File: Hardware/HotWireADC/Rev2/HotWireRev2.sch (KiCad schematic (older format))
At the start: 42 parts

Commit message: added footprints to schematic
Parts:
- added CON1: BARREL_JACK, Connect:JACK_ALIM, symbol BARREL_JACK
- added P1, P2, P3, P4: BNC, Connect:bnc-ci, symbol BNC
- added P5: CONN_02X06, Socket_Strips:Socket_Strip_Straight_2x06, symbol CONN_02X06
- C1, C10, C11, C13, C14, C15, C16, C17, C2, C3, C4, C5, C6, C7, C8: renamed from C?; footprint (none) -> Capacitors_SMD:C_1206_HandSoldering
- C12, C9: renamed from C?; footprint (none) -> Capacitors_Tantalum_SMD:TantalC_SizeU_EIA-6032
- JP1, JP3, JP4: renamed from JP?; footprint (none) -> Socket_Strips:Socket_Strip_Straight_1x03
- JP2: renamed from JP?; footprint (none) -> Socket_Strips:Socket_Strip_Straight_1x02
- R1, R10, R11, R2, R3, R4, R5, R6, R7, R8, R9: renamed from R?; footprint (none) -> Resistors_SMD:R_1206_HandSoldering
- SW1: renamed from SW?; footprint (none) -> Buttons_Switches_SMD:SW_SPST_EVPBF
- U1, U2, U3, U4, U8: renamed from U?; footprint (none) -> TO_SOT_Packages_SMD:SOT-23-5
- U5: renamed from U?; footprint (none) -> Housings_SSOP:TSSOP-24_4.4x7.8mm_Pitch0.65mm
- U6: renamed from U?; value 78L05 -> TL750L05; footprint (none) -> TO_SOT_Packages_THT:TO-92_Molded_Wide_Oval
- U7: renamed from U?; value 78L05 -> L78S05; footprint (none) -> TO_SOT_Packages_THT:TO-220_Neutral123_Vertical_LargePads
- U9: renamed from U?; footprint (none) -> SMD_Packages:SOIC-8-N
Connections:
- net EOC/~INT~/CDI is gone; now on net EXT_REF: U5.9 (EOC/~INT~/CDI)
- net GNDD is gone; now on net GNDA: C6.2, C8.2, SW1.2, U5.14 (DGND)
- net +3V3: now also P5.11 (P11), P5.12 (P12)
- net +5VA: now also U8.2 (V-)
- net EXT_REF: now also P5.7 (P7)
- net FS/~CS: now also P5.6 (P6)
- net GNDA: now also U8.5 (V+), CON1.2, CON1.3, P1.2 (Ext), P2.2 (Ext), P3.2 (Ext), P4.2 (Ext), P5.10 (P10), P5.9 (P9)
- net IN1: now also P2.1 (In)
- net IN2: now also P1.1 (In)
- net IN3: now also P4.1 (In)
- net IN4: now also P3.1 (In)
- net SCLK: now also P5.5 (P5)
- net SDI: now also P5.3 (P3)
- net SDO: now also P5.4 (P4)
- net VCC: now also CON1.1
- net ~CONVST: now also P5.2 (P2)
- net ~RESET: now also P5.1 (P1)
- no-connect marks 4 -> 6
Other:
- note added: "LOW CURRENT MODE"
- note added: "OPTIONAL - HIGH CURRENT MODE"

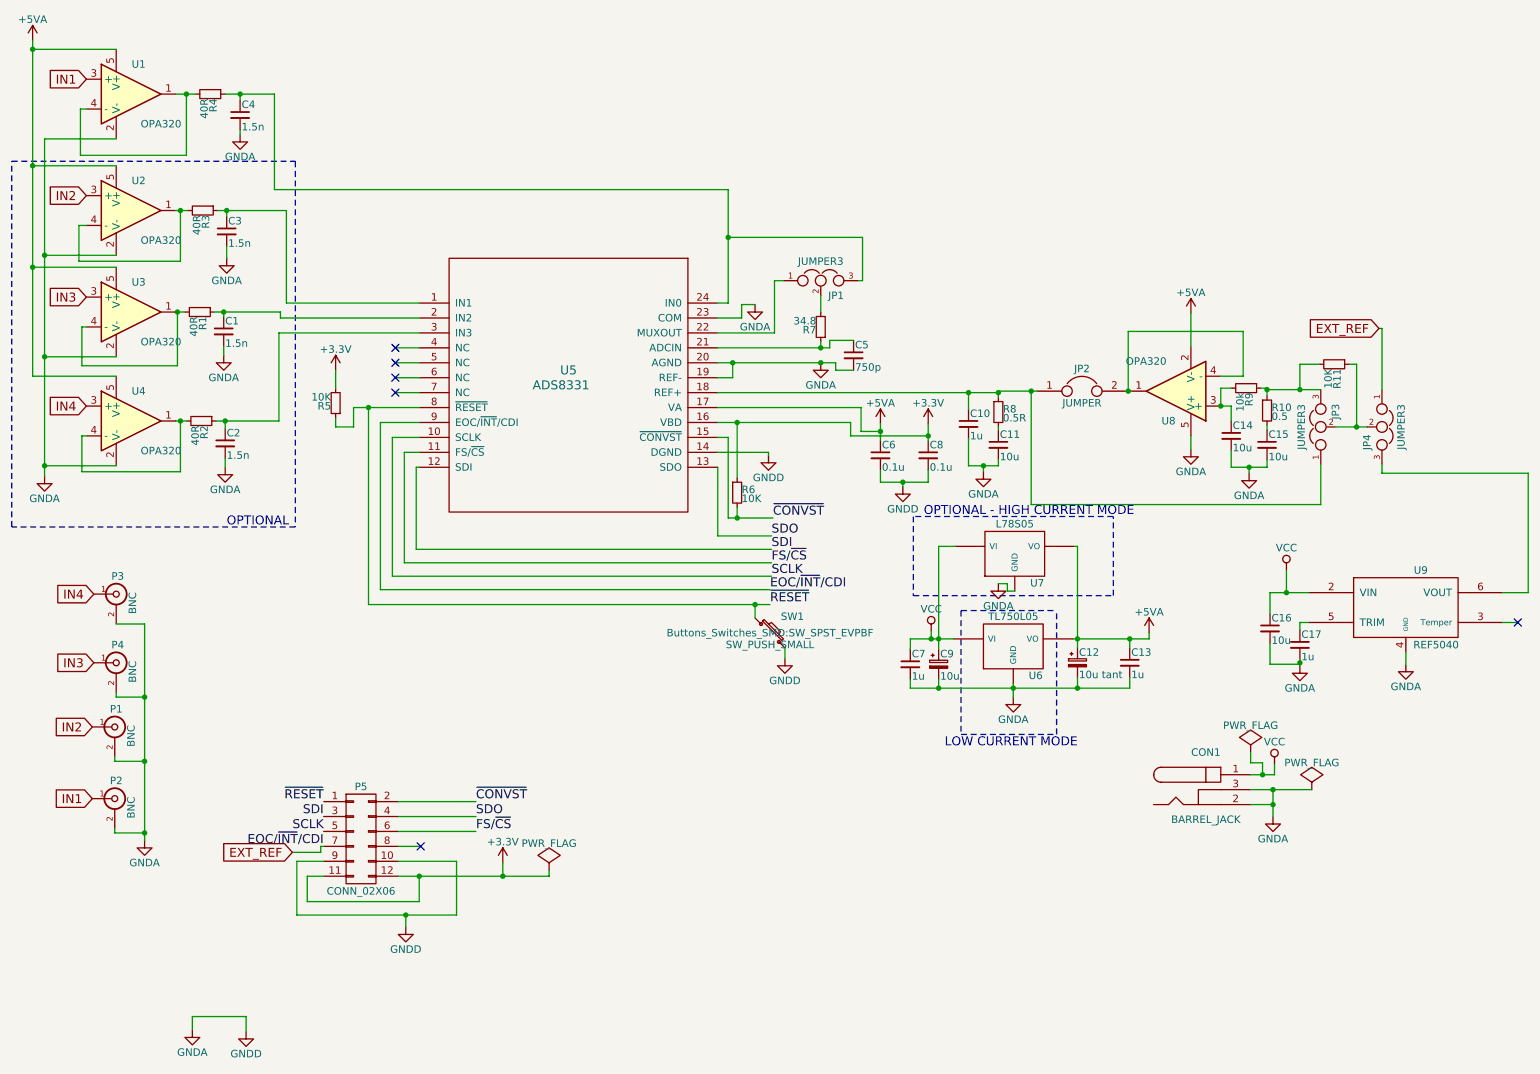
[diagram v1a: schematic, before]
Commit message: created intial PCB layout
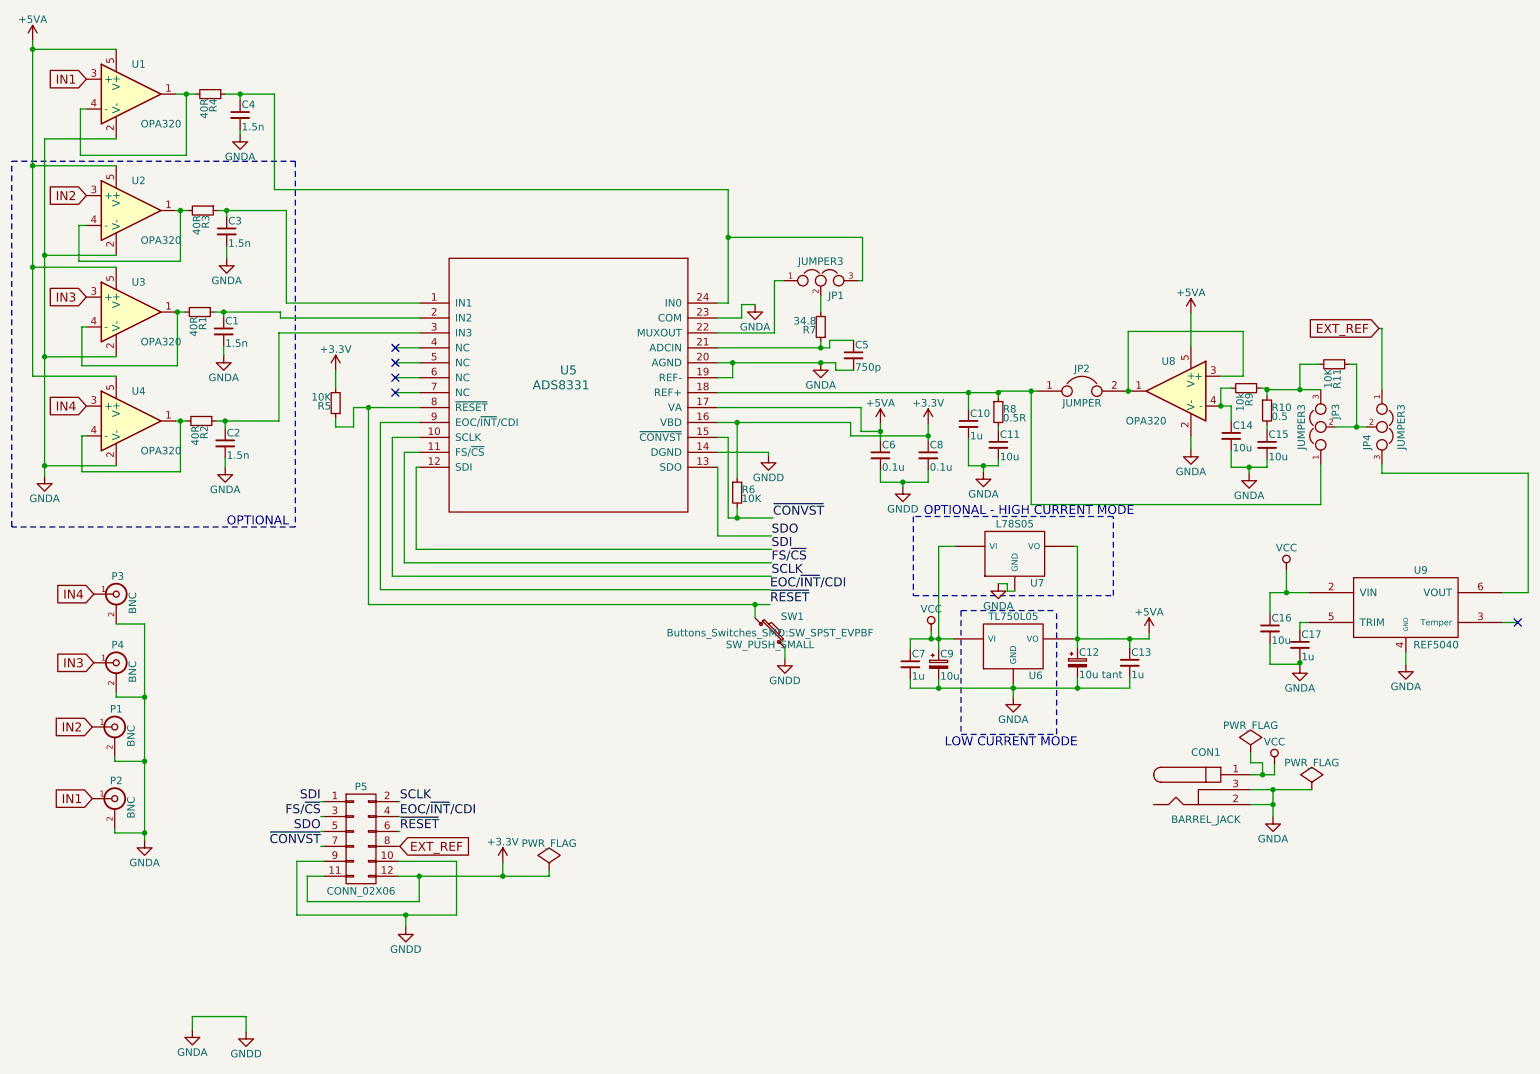
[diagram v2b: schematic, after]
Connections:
- net +5VA: now also U8.5 (V+); no longer U8.2 (V-)
- net EXT_REF: now also P5.8 (P8); no longer P5.7 (P7), U5.9 (EOC/~INT~/CDI)
- net FS/~CS: now also P5.3 (P3); no longer P5.6 (P6)
- net GNDA: now also U8.2 (V-); no longer U8.5 (V+)
- net SCLK: now also P5.2 (P2); no longer P5.5 (P5)
- net SDI: now also P5.1 (P1); no longer P5.3 (P3)
- net SDO: now also P5.5 (P5); no longer P5.4 (P4)
- net ~CONVST: now also P5.7 (P7); no longer P5.2 (P2)
- net ~RESET: now also P5.6 (P6); no longer P5.1 (P1)
- net at JP2.2, U8.1: now also U8.3 (+); no longer U8.4 (-)
- net at C14.1, R9.2: now also U8.4 (-); no longer U8.3 (+)
- new net EOC/~INT~/CDI: P5.4 (P4), U5.9 (EOC/~INT~/CDI)
- no-connect marks 6 -> 5
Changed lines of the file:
@@
 F 3 "" H 8360 3230 50  0000 C CNN
 	1    8310 3030
-	-1   0    0    1
+	-1   0    0    -1
 $EndComp
 Wire Wire Line
@@
 $EndComp
 Wire Wire Line
-	3100 5780 3620 5780
-Wire Wire Line
-	3100 5880 3620 5880
+	3100 5780 3110 5780
+Wire Wire Line
+	3100 5880 3110 5880
 Wire Wire Line
 	3100 6280 4110 6280
@@
 	3100 6180 3490 6180
 Wire Wire Line
-	3490 6180 3490 6540
+	3490 6540 3490 6180
 Wire Wire Line
 	2420 6540 2420 6180
@@
 	2080 7220 2080 7320
 Wire Wire Line
-	3490 6540 2420 6540
-Text Label 3620 5780 0    60   ~ 0
+	2420 6540 3490 6540
+Text Label 2580 6080 2    60   ~ 0
 ~CONVST
-Text Label 2600 5780 2    60   ~ 0
+Text Label 3110 5980 0    60   ~ 0
 ~RESET
-Text Label 3620 5880 0    60   ~ 0
+Text Label 2580 5980 2    60   ~ 0
 SDO
-Text Label 2600 5880 2    60   ~ 0
+Text Label 2580 5780 2    60   ~ 0
 SDI
-Text Label 3620 5980 0    60   ~ 0
+Text Label 2580 5880 2    60   ~ 0
 FS/~CS
-Text Label 2600 5980 2    60   ~ 0
+Text Label 3110 5780 0    60   ~ 0
 SCLK
-Text Label 2600 6080 2    60   ~ 0
+Text Label 3110 5880 0    60   ~ 0
 EOC/~INT~/CDI
 Wire Wire Line
-	3100 5980 3620 5980
-Wire Wire Line
-	3100 6080 3250 6080
-Wire Wire Line
-	2600 6080 2580 6080
-NoConn ~ 3250 6080
+	3100 5980 3110 5980
+Wire Wire Line
+	3100 6080 3110 6080
 Wire Wire Line
 	10500 4580 10600 4580
 NoConn ~ 10600 4580
-Text GLabel 2390 6120 0    60   Input ~ 0
+Text GLabel 3110 6080 2    60   Input ~ 0
 EXT_REF
-Wire Wire Line
-	2390 6120 2580 6120
-Wire Wire Line
-	2580 6120 2580 6080
 $Comp
 L GNDA #PWR034
@@
 Text Notes 6760 5420 0    60   ~ 0
 LOW CURRENT MODE
+Wire Wire Line
+	2600 5880 2580 5880
+Wire Wire Line
+	2580 5980 2600 5980
+Wire Wire Line
+	2600 6080 2580 6080
+Wire Wire Line
+	2600 5780 2580 5780
 $EndSCHEMATC

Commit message: moved external reference to BNC connector & tidied layout
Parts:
- added P6: BNC, Connect:bnc-ci, symbol BNC
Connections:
- net EXT_REF: now also P6.1 (In); no longer P5.8 (P8)
- net GNDA: now also P6.2 (Ext)
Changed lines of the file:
@@
 	5240 2740 5990 2740
 $Comp
-L GNDA #PWR01
+L GNDA #PWR14
 U 1 1 56E3F601
 P 5490 2450
-F 0 "#PWR01" H 5490 2200 50  0001 C CNN
+F 0 "#PWR14" H 5490 2200 50  0001 C CNN
 F 1 "GNDA" H 5490 2300 50  0000 C CNN
 F 2 "" H 5490 2450 50  0000 C CNN
@@
 	2040 1040 2040 1080
 $Comp
-L GNDA #PWR02
+L GNDA #PWR8
 U 1 1 56E40FF4
 P 2040 1310
-F 0 "#PWR02" H 2040 1060 50  0001 C CNN
+F 0 "#PWR8" H 2040 1060 50  0001 C CNN
 F 1 "GNDA" H 2040 1160 50  0000 C CNN
 F 2 "" H 2040 1310 50  0000 C CNN
@@
 $EndComp
 $Comp
-L GNDA #PWR03
+L GNDA #PWR7
 U 1 1 56E41956
 P 1950 2140
-F 0 "#PWR03" H 1950 1890 50  0001 C CNN
+F 0 "#PWR7" H 1950 1890 50  0001 C CNN
 F 1 "GNDA" H 1950 1990 50  0000 C CNN
 F 2 "" H 1950 2140 50  0000 C CNN
@@
 $EndComp
 $Comp
-L GNDA #PWR04
+L GNDA #PWR5
 U 1 1 56E41985
 P 1930 2790
-F 0 "#PWR04" H 1930 2540 50  0001 C CNN
+F 0 "#PWR5" H 1930 2540 50  0001 C CNN
 F 1 "GNDA" H 1930 2640 50  0000 C CNN
 F 2 "" H 1930 2790 50  0000 C CNN
@@
 $EndComp
 $Comp
-L GNDA #PWR05
+L GNDA #PWR6
 U 1 1 56E41CBD
 P 1940 3540
-F 0 "#PWR05" H 1940 3290 50  0001 C CNN
+F 0 "#PWR6" H 1940 3290 50  0001 C CNN
 F 1 "GNDA" H 1940 3390 50  0000 C CNN
 F 2 "" H 1940 3540 50  0000 C CNN
@@
 Connection ~ 730  2800
 $Comp
-L GNDA #PWR06
+L GNDA #PWR2
 U 1 1 56E467C4
 P 730 3600
-F 0 "#PWR06" H 730 3350 50  0001 C CNN
+F 0 "#PWR2" H 730 3350 50  0001 C CNN
 F 1 "GNDA" H 730 3450 50  0000 C CNN
 F 2 "" H 730 3600 50  0000 C CNN
@@
 IN4
 $Comp
-L +5VA #PWR07
+L +5VA #PWR1
 U 1 1 56E47E9A
 P 650 680
-F 0 "#PWR07" H 650 530 50  0001 C CNN
+F 0 "#PWR1" H 650 530 50  0001 C CNN
 F 1 "+5VA" H 650 820 50  0000 C CNN
 F 2 "" H 650 680 50  0000 C CNN
@@
 Connection ~ 650  740
 $Comp
-L GNDA #PWR08
+L GNDA #PWR17
 U 1 1 56E4881E
 P 5930 2840
-F 0 "#PWR08" H 5930 2590 50  0001 C CNN
+F 0 "#PWR17" H 5930 2590 50  0001 C CNN
 F 1 "GNDA" H 5930 2690 50  0000 C CNN
 F 2 "" H 5930 2840 50  0000 C CNN
@@
 ~RESET
 $Comp
-L GNDD #PWR09
+L GNDD #PWR19
 U 1 1 56E4A9FC
 P 6480 3670
-F 0 "#PWR09" H 6480 3420 50  0001 C CNN
+F 0 "#PWR19" H 6480 3420 50  0001 C CNN
 F 1 "GNDD" H 6480 3520 50  0000 C CNN
 F 2 "" H 6480 3670 50  0000 C CNN
@@
 $EndComp
 $Comp
-L GNDD #PWR010
+L GNDD #PWR16
 U 1 1 56E51293
 P 5690 4820
-F 0 "#PWR010" H 5690 4570 50  0001 C CNN
+F 0 "#PWR16" H 5690 4570 50  0001 C CNN
 F 1 "GNDD" H 5690 4670 50  0000 C CNN
 F 2 "" H 5690 4820 50  0000 C CNN
@@
 	5690 4750 5690 4820
 $Comp
-L +3.3V #PWR011
+L +3.3V #PWR20
 U 1 1 56E51B59
 P 6650 3250
-F 0 "#PWR011" H 6650 3100 50  0001 C CNN
+F 0 "#PWR20" H 6650 3100 50  0001 C CNN
 F 1 "+3.3V" H 6650 3390 50  0000 C CNN
 F 2 "" H 6650 3250 50  0000 C CNN
@@
 $EndComp
 $Comp
-L +3.3V #PWR012
+L +3.3V #PWR10
 U 1 1 56E51F06
 P 2680 2890
-F 0 "#PWR012" H 2680 2740 50  0001 C CNN
+F 0 "#PWR10" H 2680 2740 50  0001 C CNN
 F 1 "+3.3V" H 2680 3030 50  0000 C CNN
 F 2 "" H 2680 2890 50  0000 C CNN
@@
 $EndComp
 $Comp
-L +5VA #PWR013
+L +5VA #PWR18
 U 1 1 56E54038
 P 6330 3250
-F 0 "#PWR013" H 6330 3100 50  0001 C CNN
+F 0 "#PWR18" H 6330 3100 50  0001 C CNN
 F 1 "+5VA" H 6330 3390 50  0000 C CNN
 F 2 "" H 6330 3250 50  0000 C CNN
@@
 	5310 3340 5310 3880
 $Comp
-L GNDD #PWR014
+L GNDD #PWR15
 U 1 1 56E56979
 P 5580 3460
-F 0 "#PWR014" H 5580 3210 50  0001 C CNN
+F 0 "#PWR15" H 5580 3210 50  0001 C CNN
 F 1 "GNDD" H 5580 3310 50  0000 C CNN
 F 2 "" H 5580 3460 50  0000 C CNN
@@
 Connection ~ 6650 3330
 $Comp
-L GNDA #PWR015
+L GNDA #PWR22
 U 1 1 56E5B194
 P 7020 3570
-F 0 "#PWR015" H 7020 3320 50  0001 C CNN
+F 0 "#PWR22" H 7020 3320 50  0001 C CNN
 F 1 "GNDA" H 7020 3420 50  0000 C CNN
 F 2 "" H 7020 3570 50  0000 C CNN
@@
 	8920 3540 8920 3490
 $Comp
-L GNDA #PWR016
+L GNDA #PWR28
 U 1 1 56E66816
 P 8800 3580
-F 0 "#PWR016" H 8800 3330 50  0001 C CNN
+F 0 "#PWR28" H 8800 3330 50  0001 C CNN
 F 1 "GNDA" H 8800 3430 50  0000 C CNN
 F 2 "" H 8800 3580 50  0000 C CNN
@@
 $EndComp
 $Comp
-L GNDA #PWR017
+L GNDA #PWR33
 U 1 1 56E6DC74
 P 9850 4860
-F 0 "#PWR017" H 9850 4610 50  0001 C CNN
+F 0 "#PWR33" H 9850 4610 50  0001 C CNN
 F 1 "GNDA" H 9850 4710 50  0000 C CNN
 F 2 "" H 9850 4860 50  0000 C CNN
@@
 $EndComp
 $Comp
-L GNDA #PWR018
+L GNDA #PWR32
 U 1 1 56E6FEF4
 P 9140 4870
-F 0 "#PWR018" H 9140 4620 50  0001 C CNN
+F 0 "#PWR32" H 9140 4620 50  0001 C CNN
 F 1 "GNDA" H 9140 4720 50  0000 C CNN
 F 2 "" H 9140 4870 50  0000 C CNN
@@
 Connection ~ 9140 4850
 $Comp
-L VCC #PWR019
+L VCC #PWR31
 U 1 1 56E73E38
 P 9050 4230
-F 0 "#PWR019" H 9050 4080 50  0001 C CNN
+F 0 "#PWR31" H 9050 4080 50  0001 C CNN
 F 1 "VCC" H 9050 4380 50  0000 C CNN
 F 2 "" H 9050 4230 50  0000 C CNN
@@
 $EndComp
 $Comp
-L +5VA #PWR020
+L +5VA #PWR25
 U 1 1 56E766A8
 P 8130 4650
-F 0 "#PWR020" H 8130 4500 50  0001 C CNN
+F 0 "#PWR25" H 8130 4500 50  0001 C CNN
 F 1 "+5VA" H 8130 4790 50  0000 C CNN
 F 2 "" H 8130 4650 50  0000 C CNN
@@
 $EndComp
 $Comp
-L VCC #PWR021
+L VCC #PWR21
 U 1 1 56E76726
 P 6670 4640
-F 0 "#PWR021" H 6670 4490 50  0001 C CNN
+F 0 "#PWR21" H 6670 4490 50  0001 C CNN
 F 1 "VCC" H 6670 4790 50  0000 C CNN
 F 2 "" H 6670 4640 50  0000 C CNN
@@
 Connection ~ 8000 4690
 $Comp
-L GNDA #PWR022
+L GNDA #PWR24
 U 1 1 56E77814
 P 7220 5080
-F 0 "#PWR022" H 7220 4830 50  0001 C CNN
+F 0 "#PWR24" H 7220 4830 50  0001 C CNN
 F 1 "GNDA" H 7220 4930 50  0000 C CNN
 F 2 "" H 7220 5080 50  0000 C CNN
@@
 	6830 4070 6720 4070
 $Comp
-L GNDA #PWR023
+L GNDA #PWR23
 U 1 1 56E7EB42
 P 7120 4320
-F 0 "#PWR023" H 7120 4070 50  0001 C CNN
+F 0 "#PWR23" H 7120 4070 50  0001 C CNN
 F 1 "GNDA" H 7120 4170 50  0000 C CNN
 F 2 "" H 7120 4320 50  0000 C CNN
@@
 IN1
 $Comp
-L GNDA #PWR024
+L GNDA #PWR3
 U 1 1 56E89E10
 P 1400 6040
-F 0 "#PWR024" H 1400 5790 50  0001 C CNN
+F 0 "#PWR3" H 1400 5790 50  0001 C CNN
 F 1 "GNDA" H 1400 5890 50  0000 C CNN
 F 2 "" H 1400 6040 50  0000 C CNN
@@
 	3100 6180 3490 6180
 Wire Wire Line
-	3490 6540 3490 6180
+	3490 6180 3490 6540
 Wire Wire Line
 	2420 6540 2420 6180
@@
 Connection ~ 3240 6280
 $Comp
-L GNDA #PWR025
+L GNDA #PWR4
 U 1 1 56E8E642
 P 1720 7310
-F 0 "#PWR025" H 1720 7060 50  0001 C CNN
+F 0 "#PWR4" H 1720 7060 50  0001 C CNN
 F 1 "GNDA" H 1720 7160 50  0000 C CNN
 F 2 "" H 1720 7310 50  0000 C CNN
@@
 $EndComp
 $Comp
-L +3.3V #PWR026
+L +3.3V #PWR12
 U 1 1 56E902E0
 P 3800 6190
-F 0 "#PWR026" H 3800 6040 50  0001 C CNN
+F 0 "#PWR12" H 3800 6040 50  0001 C CNN
 F 1 "+3.3V" H 3800 6330 50  0000 C CNN
 F 2 "" H 3800 6190 50  0000 C CNN
@@
 $EndComp
 $Comp
-L GNDA #PWR027
+L GNDA #PWR29
 U 1 1 56E93599
 P 8960 5880
-F 0 "#PWR027" H 8960 5630 50  0001 C CNN
+F 0 "#PWR29" H 8960 5630 50  0001 C CNN
 F 1 "GNDA" H 8960 5730 50  0000 C CNN
 F 2 "" H 8960 5880 50  0000 C CNN
@@
 Connection ~ 8960 5800
 $Comp
-L VCC #PWR028
+L VCC #PWR30
 U 1 1 56E941B0
 P 8970 5530
-F 0 "#PWR028" H 8970 5380 50  0001 C CNN
+F 0 "#PWR30" H 8970 5380 50  0001 C CNN
 F 1 "VCC" H 8970 5680 50  0000 C CNN
 F 2 "" H 8970 5530 50  0000 C CNN
@@
 	8970 5600 8970 5530
 $Comp
-L PWR_FLAG #FLG029
+L PWR_FLAG #FLG2
 U 1 1 56E94ED5
 P 8810 5450
-F 0 "#FLG029" H 8810 5545 50  0001 C CNN
+F 0 "#FLG2" H 8810 5545 50  0001 C CNN
 F 1 "PWR_FLAG" H 8810 5630 50  0000 C CNN
 F 2 "" H 8810 5450 50  0000 C CNN
@@
 $EndComp
 $Comp
-L PWR_FLAG #FLG030
+L PWR_FLAG #FLG3
 U 1 1 56E95487
 P 9220 5700
-F 0 "#FLG030" H 9220 5795 50  0001 C CNN
+F 0 "#FLG3" H 9220 5795 50  0001 C CNN
 F 1 "PWR_FLAG" H 9220 5880 50  0000 C CNN
 F 2 "" H 9220 5700 50  0000 C CNN
@@
 $EndComp
 $Comp
-L PWR_FLAG #FLG031
+L PWR_FLAG #FLG1
 U 1 1 56E957F2
 P 4110 6240
-F 0 "#FLG031" H 4110 6335 50  0001 C CNN
+F 0 "#FLG1" H 4110 6335 50  0001 C CNN
 F 1 "PWR_FLAG" H 4110 6420 50  0000 C CNN
 F 2 "" H 4110 6240 50  0000 C CNN
@@
 Connection ~ 8890 5600
 $Comp
-L GNDD #PWR032
+L GNDD #PWR11
 U 1 1 56E9B38E
 P 3150 6620
-F 0 "#PWR032" H 3150 6370 50  0001 C CNN
+F 0 "#PWR11" H 3150 6370 50  0001 C CNN
 F 1 "GNDD" H 3150 6470 50  0000 C CNN
 F 2 "" H 3150 6620 50  0000 C CNN
@@
 Connection ~ 3150 6540
 $Comp
-L GNDD #PWR033
+L GNDD #PWR9
 U 1 1 56E9D5EC
 P 2080 7320
-F 0 "#PWR033" H 2080 7070 50  0001 C CNN
+F 0 "#PWR9" H 2080 7070 50  0001 C CNN
 F 1 "GNDD" H 2080 7170 50  0000 C CNN
 F 2 "" H 2080 7320 50  0000 C CNN
@@
 	2080 7220 2080 7320
 Wire Wire Line
-	2420 6540 3490 6540
+	3490 6540 2420 6540
 Text Label 2580 6080 2    60   ~ 0
 ~CONVST
@@
 	10500 4580 10600 4580
 NoConn ~ 10600 4580
-Text GLabel 3110 6080 2    60   Input ~ 0
+Text GLabel 4800 5920 0    60   Input ~ 0
 EXT_REF
 $Comp
-L GNDA #PWR034
+L GNDA #PWR27
 U 1 1 56EAC6C3
 P 8410 3420
-F 0 "#PWR034" H 8410 3170 50  0001 C CNN
+F 0 "#PWR27" H 8410 3170 50  0001 C CNN
 F 1 "GNDA" H 8410 3270 50  0000 C CNN
 F 2 "" H 8410 3420 50  0000 C CNN
@@
 	8410 3330 8410 3420
 $Comp
-L +5VA #PWR035
+L +5VA #PWR26
 U 1 1 56EAD0BF
 P 8410 2510
-F 0 "#PWR035" H 8410 2360 50  0001 C CNN
+F 0 "#PWR26" H 8410 2360 50  0001 C CNN
 F 1 "+5VA" H 8410 2650 50  0000 C CNN
 F 2 "" H 8410 2510 50  0000 C CNN
@@
 Wire Wire Line
 	2600 5780 2580 5780
+$Comp
+L BNC P6
+U 1 1 56E5B816
+P 4950 5920
+F 0 "P6" H 4960 6040 50  0000 C CNN
+F 1 "BNC" V 5060 5860 50  0000 C CNN
+F 2 "Connect:bnc-ci" H 4950 5920 50  0001 C CNN
+F 3 "" H 4950 5920 50  0000 C CNN
+	1    4950 5920
+	1    0    0    -1
+$EndComp
+$Comp
+L GNDA #PWR13
+U 1 1 56E5C590
+P 4950 6120
+F 0 "#PWR13" H 4950 5870 50  0001 C CNN
+F 1 "GNDA" H 4950 5970 50  0000 C CNN
+F 2 "" H 4950 6120 50  0000 C CNN
+F 3 "" H 4950 6120 50  0000 C CNN
+	1    4950 6120
+	1    0    0    -1
+$EndComp
 $EndSCHEMATC

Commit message: updated regulator footprint and removed additional regulator
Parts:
- removed U6: TL750L05, TO_SOT_Packages_THT:TO-92_Molded_Wide_Oval, symbol 78L05
- U7: footprint TO_SOT_Packages_THT:TO-220_Neutral123_Vertical_LargePads -> CustomFootprints:TO-220_REGULATORVIGNDVO_Vertical_LargePads
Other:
- note removed: "LOW CURRENT MODE"
- note removed: "OPTIONAL - HIGH CURRENT MODE"
- moved on the sheet: U7
